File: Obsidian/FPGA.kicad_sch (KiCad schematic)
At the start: 45 parts, among them Q1 BSS138LT1G, Q2 BSS138LT1G, SW2 SW_DIP_x01, U1 XC7A35T-CSG325, U28 24AA256UID-I_ST

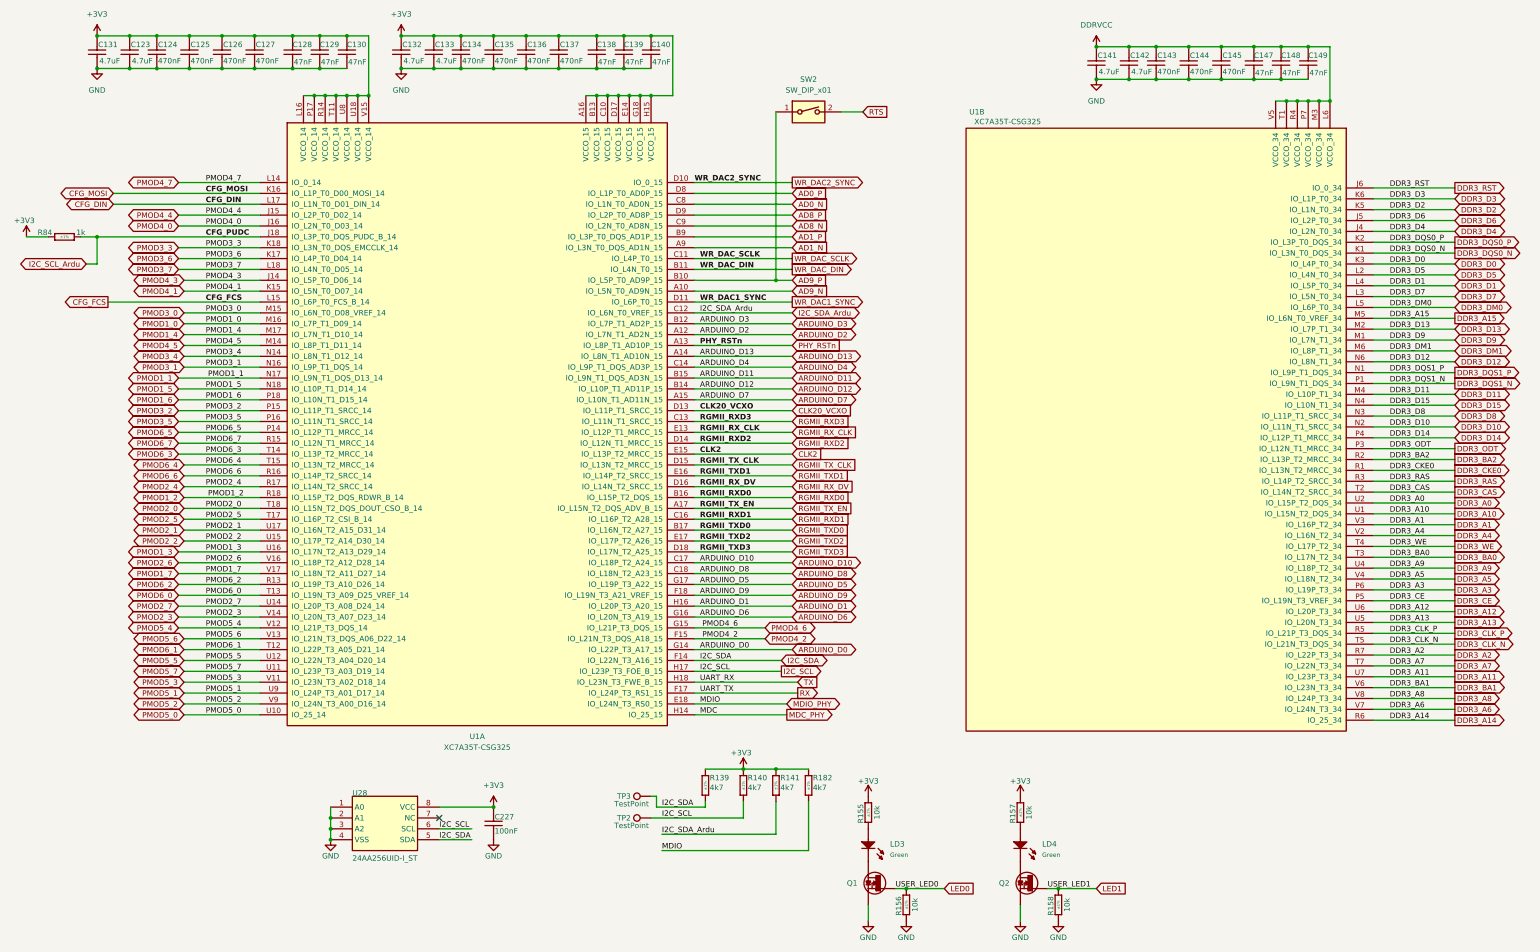
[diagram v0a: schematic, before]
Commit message: Removing unnecessary components for the interface. Adding SPIN schematic and footprint
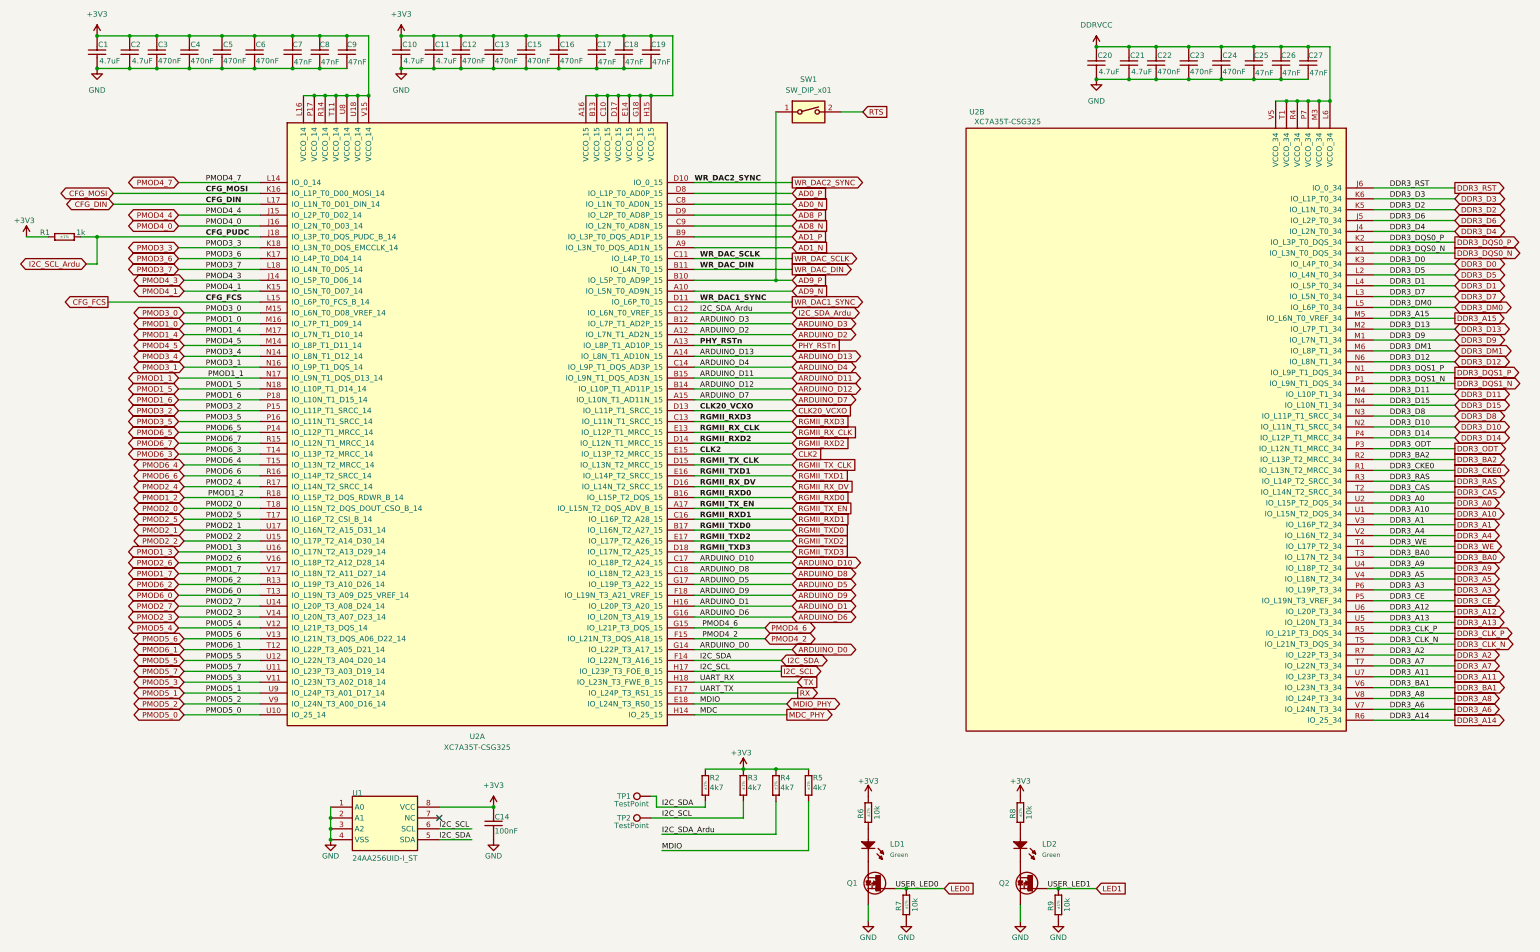
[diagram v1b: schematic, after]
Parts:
- renumbered C131 to C1, C132 to C10, C133 to C11, C134 to C12, C135 to C13, C227 to C14, C136 to C15, C137 to C16, C138 to C17, C139 to C18, C140 to C19, C123 to C2, C141 to C20, C142 to C21, C143 to C22, C144 to C23, C145 to C24, C147 to C25, C148 to C26, C149 to C27, C124 to C3, C125 to C4, C126 to C5, C127 to C6, C128 to C7, C129 to C8, C130 to C9, LD3 to LD1, LD4 to LD2, R84 to R1, R139 to R2, R140 to R3, R141 to R4, R182 to R5, R155 to R6, R156 to R7, R157 to R8, R158 to R9, SW2 to SW1, TP3 to TP1, U28 to U1, U1 to U2

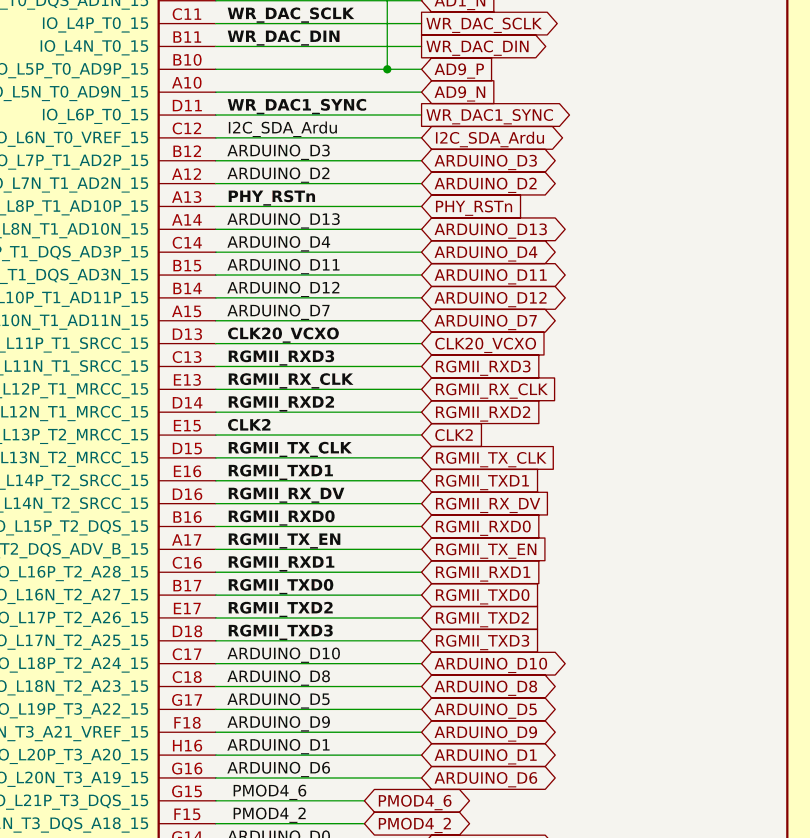
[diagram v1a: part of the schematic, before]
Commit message: adding SPIN, and 5V power for the MCU
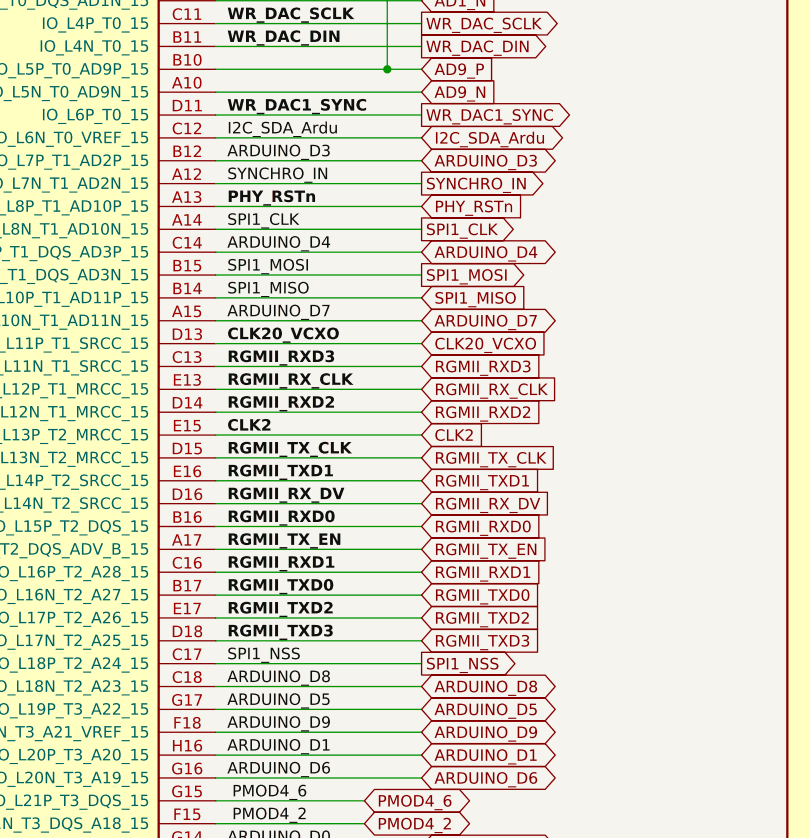
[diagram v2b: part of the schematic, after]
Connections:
- net ARDUINO_D10 renamed SPI1_NSS
- net ARDUINO_D11 renamed SPI1_MOSI
- net ARDUINO_D12 renamed SPI1_MISO
- net ARDUINO_D13 renamed SPI1_CLK
- net ARDUINO_D2 renamed SYNCHRO_IN
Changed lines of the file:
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@@
 		)
 	)
-	(label "ARDUINO_D13"
+	(label "SPI1_CLK"
 		(at 193.04 127 0)
 		(effects
@@
 		)
 	)
-	(label "ARDUINO_D11"
+	(label "SPI1_MOSI"
 		(at 193.04 132.08 0)
 		(effects
@@
 		)
 	)
-	(label "ARDUINO_D12"
+	(label "SPI1_MISO"
 		(at 193.04 134.62 0)
 		(effects
@@
 		)
 	)
-	(label "ARDUINO_D2"
+	(label "SYNCHRO_IN"
 		(at 193.04 121.92 0)
 		(effects
@@
 		)
 	)
-	(label "ARDUINO_D10"
+	(label "SPI1_NSS"
 		(at 193.04 175.26 0)
 		(effects
@@
 		)
 	)
-	(global_label "ARDUINO_D10"
-		(shape bidirectional)
+	(global_label "SPI1_NSS"
+		(shape output)
 		(at 214.63 175.26 0)
 		(fields_autoplaced yes)
@@
 		)
 		(property "Intersheetrefs" "${INTERSHEET_REFS}"
-			(at 230.4967 175.26 0)
+			(at 226.6261 175.26 0)
 			(effects
 				(font
@@
 		)
 	)
-	(global_label "ARDUINO_D2"
-		(shape bidirectional)
+	(global_label "SYNCHRO_IN"
+		(shape output)
 		(at 214.63 121.92 0)
 		(fields_autoplaced yes)
@@
 		)
 		(property "Intersheetrefs" "${INTERSHEET_REFS}"
-			(at 229.2872 121.92 0)
+			(at 229.3477 121.92 0)
 			(effects
 				(font
@@
 		)
 	)
-	(global_label "ARDUINO_D13"
-		(shape bidirectional)
+	(global_label "SPI1_CLK"
+		(shape output)
 		(at 214.63 127 0)
 		(fields_autoplaced yes)
@@
 		)
 		(property "Intersheetrefs" "${INTERSHEET_REFS}"
-			(at 230.4967 127 0)
+			(at 226.4447 127 0)
 			(effects
 				(font
@@
 		)
 	)
-	(global_label "ARDUINO_D12"
-		(shape bidirectional)
+	(global_label "SPI1_MISO"
+		(shape input)
 		(at 214.63 134.62 0)
 		(fields_autoplaced yes)
@@
 		)
 		(property "Intersheetrefs" "${INTERSHEET_REFS}"
-			(at 230.4967 134.62 0)
+			(at 227.4728 134.62 0)
 			(effects
 				(font
@@
 		)
 	)
-	(global_label "ARDUINO_D11"
-		(shape bidirectional)
+	(global_label "SPI1_MOSI"
+		(shape output)
 		(at 214.63 132.08 0)
 		(fields_autoplaced yes)
@@
 		)
 		(property "Intersheetrefs" "${INTERSHEET_REFS}"
-			(at 230.4967 132.08 0)
+			(at 227.4728 132.08 0)
 			(effects
 				(font
